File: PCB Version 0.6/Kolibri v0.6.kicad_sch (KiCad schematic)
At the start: 0 parts

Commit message: replace USB JST with pads and remove USB TVS
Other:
- sheet USB ports: added none; removed Curr_ESC, VBat_HI
- note removed: "Overvoltage Protection with TVS-Diodes in USB sheet"
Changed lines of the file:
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@@
 	(generator_version "9.0")
 	(paper "A4")
-	(text "Overvoltage Protection with TVS-Diodes in USB sheet"
-		(exclude_from_sim no)
-		(at 116.332 174.244 0)
-		(effects
-			(font
-				(size 1.27 1.27)
-			)
-		)
-	)
 	(junction
 		(at 127 81.28)
@@
 		(color 0 0 0 0)
 	)
-	(junction
-		(at 68.58 138.43)
-		(diameter 0)
-		(color 0 0 0 0)
-	)
 	(bus
 		(pts
@@
 	(wire
 		(pts
-			(xy 68.58 138.43) (xy 68.58 175.26)
-		)
-		(stroke
-			(width 0)
-			(type default)
-		)
-	)
-	(wire
-		(pts
 			(xy 63.5 80.01) (xy 81.28 80.01)
 		)
@@
 		)
 	)
-	(wire
-		(pts
-			(xy 165.1 158.75) (xy 185.42 158.75)
-		)
-		(stroke
-			(width 0)
-			(type default)
-		)
-	)
 	(bus
 		(pts
@@
 		)
 	)
-	(wire
-		(pts
-			(xy 162.56 172.72) (xy 162.56 156.21)
-		)
-		(stroke
-			(width 0)
-			(type default)
-		)
-	)
 	(bus
 		(pts
@@
 		)
 	)
-	(wire
-		(pts
-			(xy 68.58 175.26) (xy 165.1 175.26)
-		)
-		(stroke
-			(width 0)
-			(type default)
-		)
-	)
 	(bus
 		(pts
@@
 		)
 	)
-	(wire
-		(pts
-			(xy 165.1 175.26) (xy 165.1 158.75)
-		)
-		(stroke
-			(width 0)
-			(type default)
-		)
-	)
 	(bus
 		(pts
@@
 		)
 	)
-	(wire
-		(pts
-			(xy 71.12 140.97) (xy 81.28 140.97)
-		)
-		(stroke
-			(width 0)
-			(type default)
-		)
-	)
 	(bus
 		(pts
@@
 		)
 	)
-	(wire
-		(pts
-			(xy 162.56 156.21) (xy 185.42 156.21)
-		)
-		(stroke
-			(width 0)
-			(type default)
-		)
-	)
 	(bus
 		(pts
@@
 		)
 	)
-	(wire
-		(pts
-			(xy 71.12 172.72) (xy 162.56 172.72)
-		)
-		(stroke
-			(width 0)
-			(type default)
-		)
-	)
 	(bus
 		(pts
 			(xy 105.41 71.12) (xy 130.81 71.12)
-		)
-		(stroke
-			(width 0)
-			(type default)
-		)
-	)
-	(wire
-		(pts
-			(xy 71.12 140.97) (xy 71.12 172.72)
 		)
 		(stroke
@@
 			(effects
 				(font
-					(size 1.27 1.27)
-				)
-				(justify left)
-			)
-		)
-		(pin "VBat_HI" input
-			(at 185.42 156.21 180)
-			(effects
-				(font
-					(size 1.27 1.27)
-				)
-				(justify left)
-			)
-		)
-		(pin "Curr_ESC" input
-			(at 185.42 158.75 180)
-			(effects
-				(font

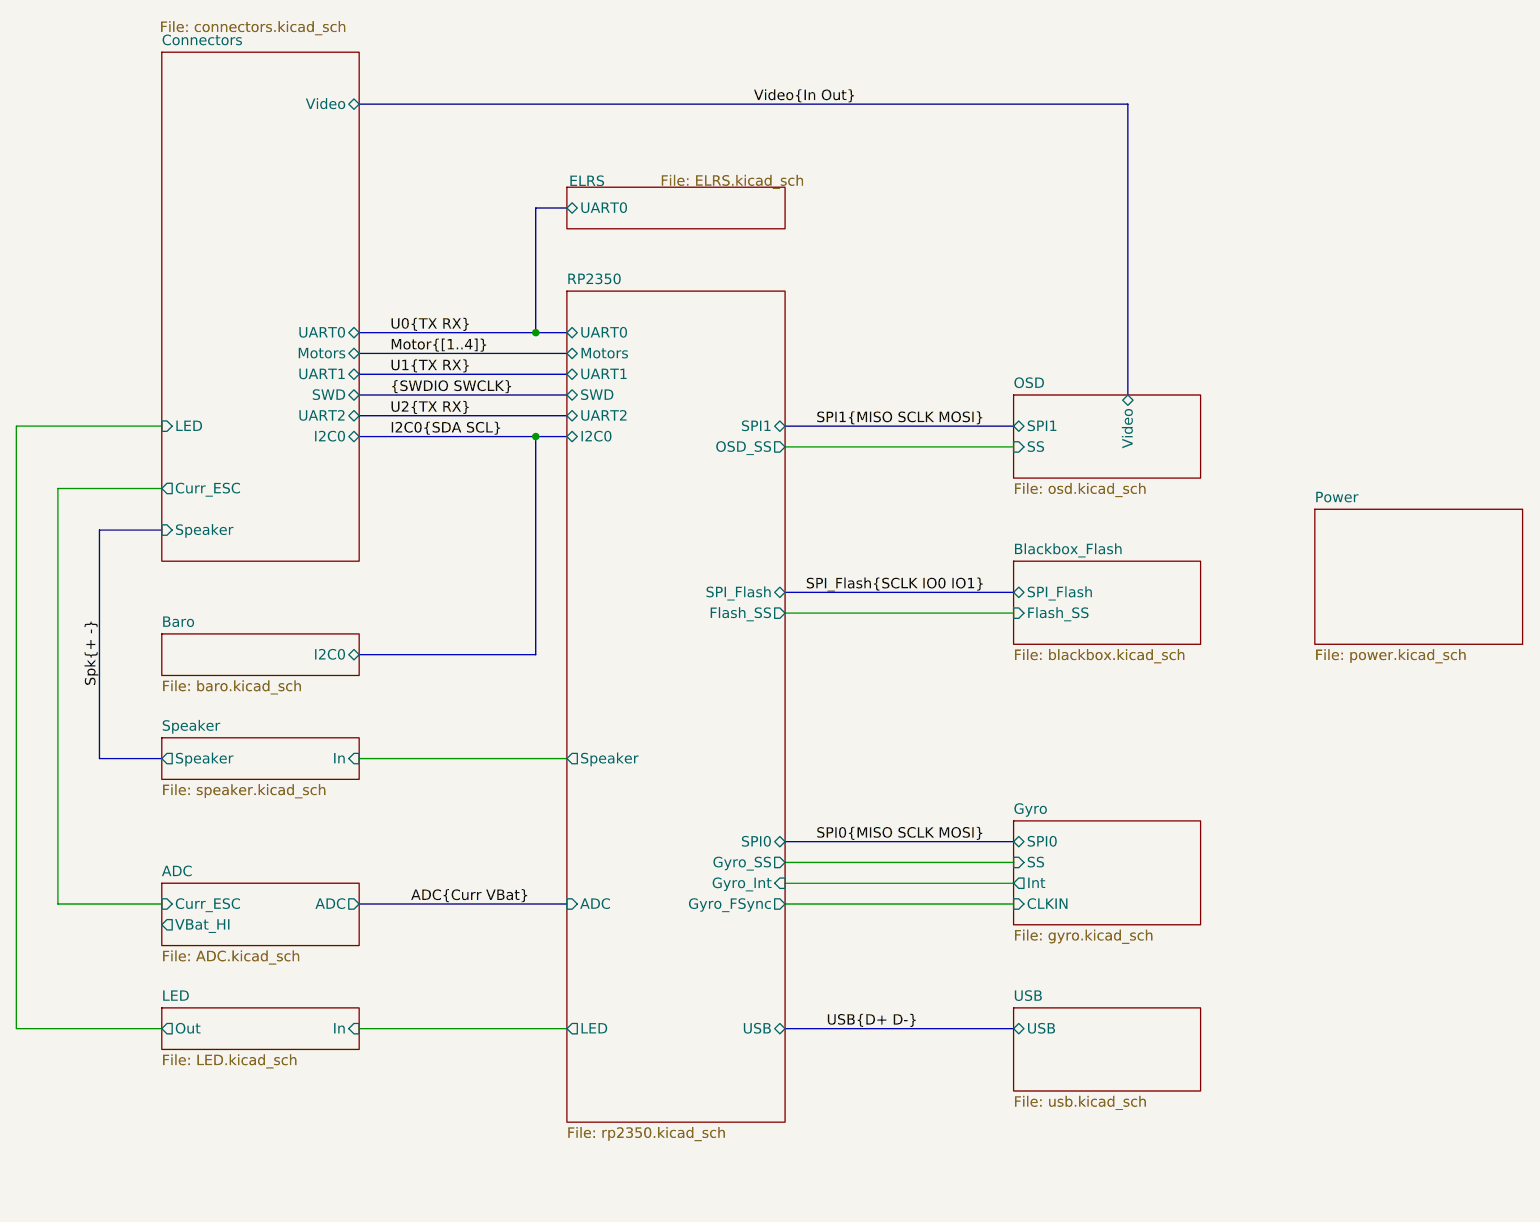
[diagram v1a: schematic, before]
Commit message: remove current sensor ADC, swap opamp, add dcdc switch
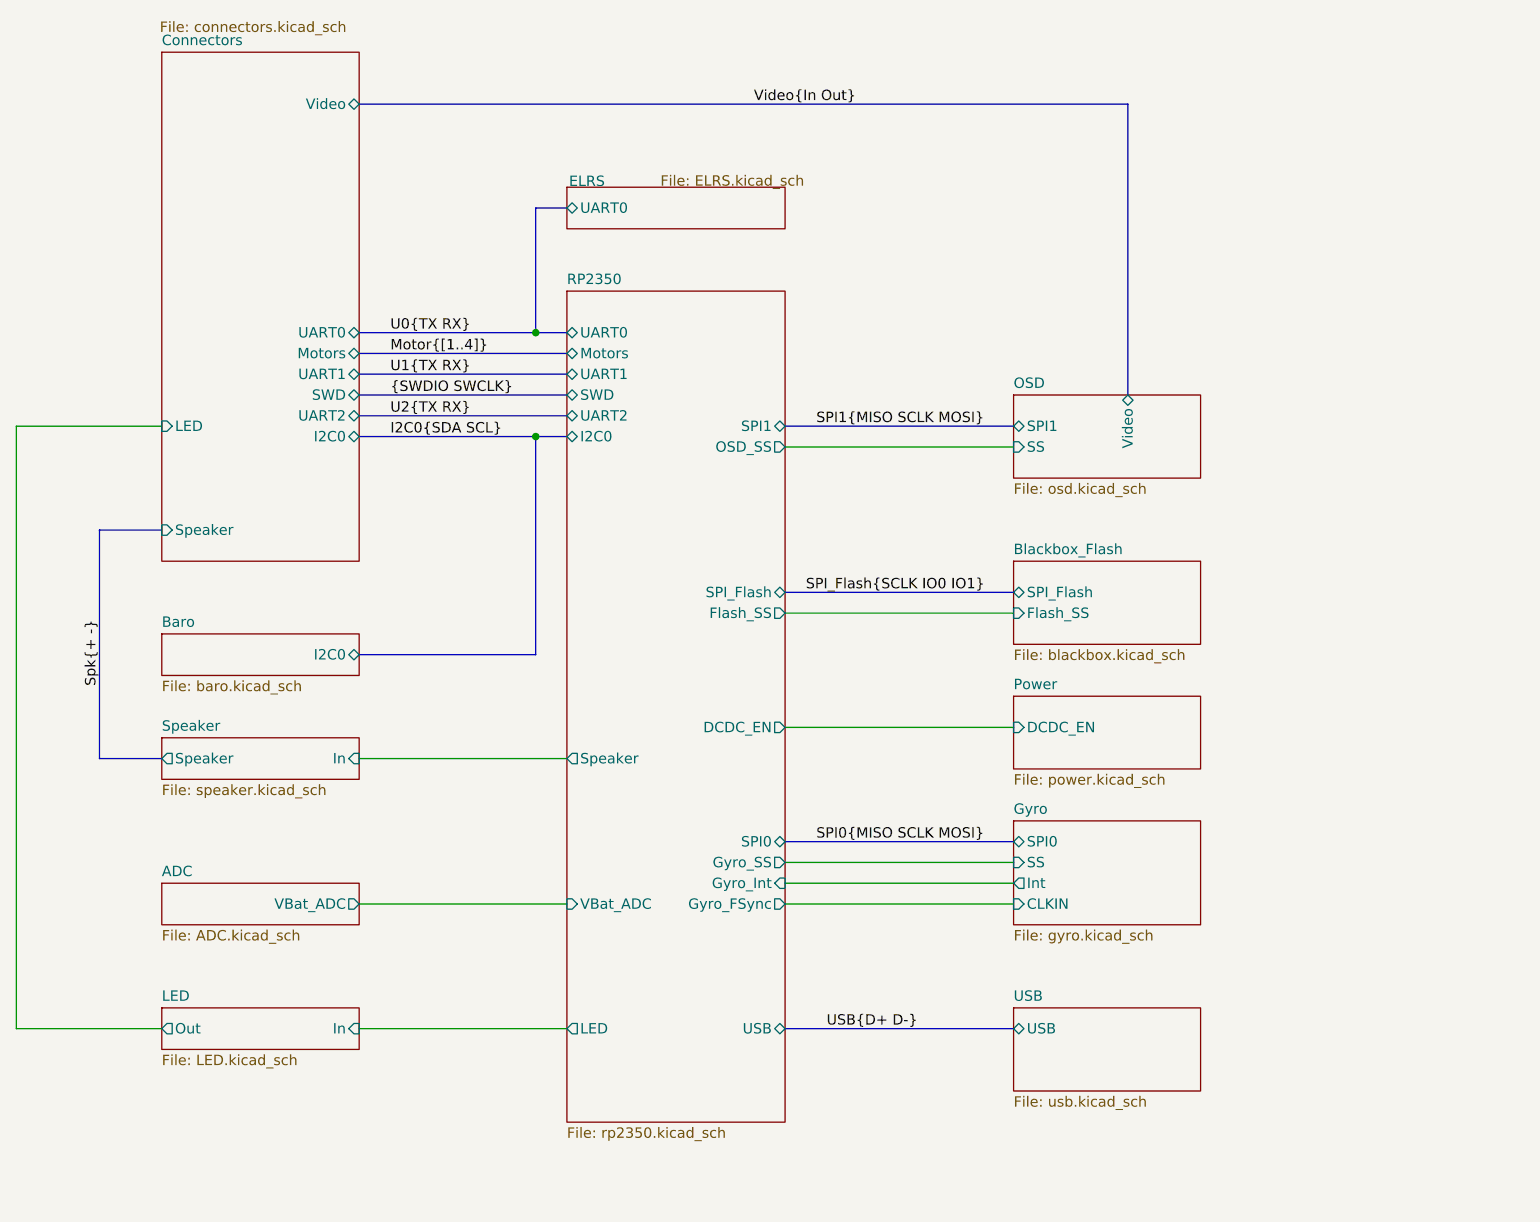
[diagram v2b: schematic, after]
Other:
- sheet ADC ports: added VBat_ADC; removed ADC, Curr_ESC, VBat_HI
- sheet Connectors ports: added none; removed Curr_ESC
- sheet Power ports: added DCDC_EN; removed none
- sheet RP2350 ports: added DCDC_EN, VBat_ADC; removed ADC

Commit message: layout first draft done
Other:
- sheet ELRS ports: added PWM; removed none
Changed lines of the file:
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@@
+	(bus
+		(pts
+			(xy 105.41 50.8) (xy 130.81 50.8)
+		)
+		(stroke
+			(width 0)
+			(type default)
+		)
+	)
 	(bus
 		(pts
@@
 			(width 0)
 			(type default)
+		)
+	)
+	(label "PWM{[1..2]}"
+		(at 109.22 50.8 0)
+		(effects
+			(font
+				(size 1.27 1.27)
+			)
+			(justify left bottom)
 		)
 	)
@@
 	)
 	(sheet
-		(at 130.81 50.8)
-		(size 26.67 5.08)
+		(at 130.81 48.26)
+		(size 26.67 7.62)
 		(exclude_from_sim no)
 		(in_bom yes)
@@
 		)
 		(property "Sheetname" "ELRS"
-			(at 131.064 50.8 0)
+			(at 131.064 48.26 0)
 			(effects
 				(font
@@
 		)
 		(property "Sheetfile" "ELRS.kicad_sch"
-			(at 142.24 49.276 0)
+			(at 142.24 46.736 0)
 			(effects
 				(font
@@
 			(effects
 				(font
+					(size 1.27 1.27)
+				)
+				(justify left)
+			)
+		)
+		(pin "PWM" output
+			(at 130.81 50.8 180)
+			(effects
+				(font

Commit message: wip
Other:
- sheet Connectors ports: added PWM; removed none
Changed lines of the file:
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@@
+			)
+		)
+		(pin "PWM" input
+			(at 105.41 50.8 0)
+			(effects
+				(font
+					(size 1.27 1.27)
+				)
+				(justify right)
 			)
 		)
